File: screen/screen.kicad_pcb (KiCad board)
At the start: 4 copper layers, 41.9 x 30 mm, 34 parts, among them J1 USB_C_Receptacle_USB2.0, J2 Conn_01x06_Female, J3 Conn_01x02_Female, J4 Conn_01x12_Female, SW1 SW_Push, SW2 SW_Push, SW3 SW_DPDT_x2, U1 ESP-12E, U2 TP4056_[C16581], U3 SPX3819M5-L-3-3

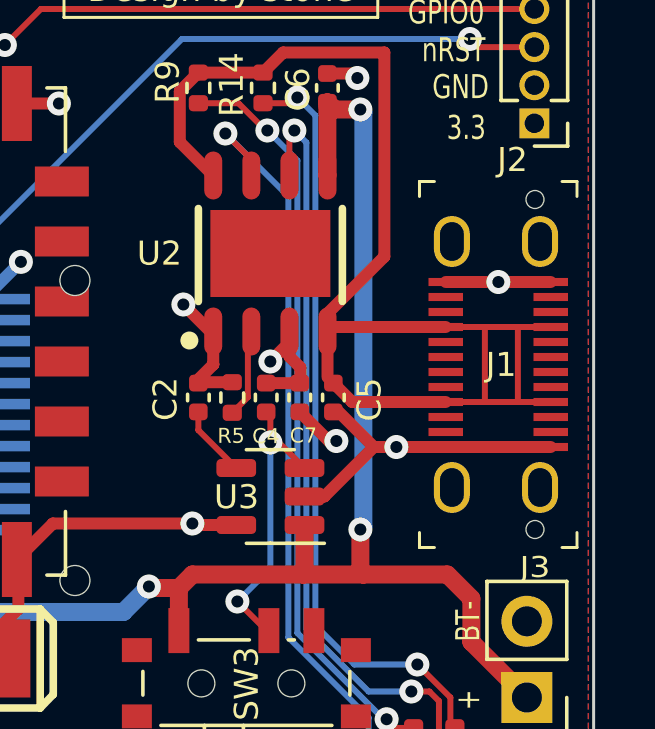
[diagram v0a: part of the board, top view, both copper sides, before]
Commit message: feat: screen v1.2
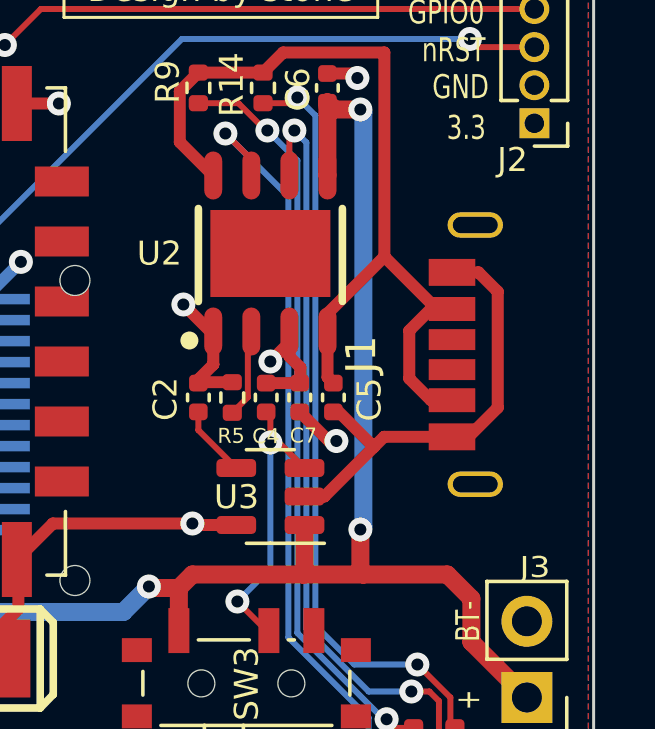
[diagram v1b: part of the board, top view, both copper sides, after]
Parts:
- J1: footprint digikey-footprints:USB-C_Female_Vert_DX07S024WJ3R400 -> My-lib-footprints:USB_C_6pin
- moved J1 2.02 mm to (135.4, 51.5), turned to 90 degrees
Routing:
- net Net-(C2-Pad2): track 42.2 -> 30.5 mm
- net GND: track 47.0 -> 47.9 mm, vias 19 -> 17
